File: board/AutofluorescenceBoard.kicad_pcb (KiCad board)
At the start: 2 copper layers, 57.2 x 45.7 mm, 41 parts, among them J1 2002411212, Q1 BSS138, U1 PAM2863ECR, U2 PAM2863ECR, U3 PAM2863ECR

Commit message: Silkscreens :)
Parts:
- added G***: LOGO, LOGO, F.Cu at (146.6, 137.6)
- added G***: LOGO, LOGO, F.Cu at (137.9, 116.7)

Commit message: Layout Changes from CDR
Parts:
- R3: value 0.3 -> 0.15
- R8: value 1K -> 10K
- moved G*** 81.4 mm to (67.5, 118.6)
- moved CR2 63.7 mm to (182.4, 130.1), turned to 90 degrees
- moved D3 61.7 mm to (185.7, 116.0)
- moved D2 56.8 mm to (180.5, 112.0)
- moved Conn1 56.5 mm to (208.7, 105.9)
- moved L2 55.9 mm to (179.8, 120.9)
- moved FanConn1 55.6 mm to (209.8, 121.0)
- moved G*** 55.6 mm to (82.6, 111.3)
- moved D1 54.2 mm to (179.2, 106.2)
- moved D4 54.2 mm to (179.4, 98.6)
- moved R1 54.2 mm to (163.8, 107.0)
- moved R4 54.2 mm to (160.7, 112.8)
- moved C1 54.2 mm to (166.9, 125.5)
- moved C3 54.2 mm to (168.9, 113.4)
- moved CR1 54.2 mm to (158.4, 118.0)
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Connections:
- J1 pad 2: Net-(J1-Pad2) -> unconnected-(J1-Pad2)
- MOSFET1 pad 5: Net-(J1-Pad2) -> GND
- MOSFET1 pad 6: Net-(J1-Pad2) -> GND
- MOSFET1 pad 7: Net-(J1-Pad2) -> GND
- MOSFET1 pad 8: Net-(J1-Pad2) -> GND
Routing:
- net Net-(J1-Pad2): track 28.6 -> 0.00 mm
- net (no net): track 0.00 -> 28.6 mm
- net Net-(D2-Pad2): track 4.06 -> 12.3 mm
- net Net-(D3-Pad2): track 5.74 -> 1.40 mm
- net White LED: track 5.69 -> 9.63 mm
- net ISET 490nm: track 39.5 -> 42.3 mm
- net ISET 405nm: track 59.9 -> 62.6 mm
- net Net-(D2-Pad1): track 7.21 -> 5.32 mm
- net ISET 365nm: track 77.1 -> 78.4 mm
- net +12V: track 179.2 -> 177.9 mm
- net Net-(D3-Pad1): track 6.24 -> 5.22 mm
- net Net-(CR2-Pad2): track 10.6 -> 9.77 mm
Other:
- board size 57.2 x 45.7 mm -> 60.3 x 48.9 mm
- board text removed: "increase width by .01 increase length by .03"

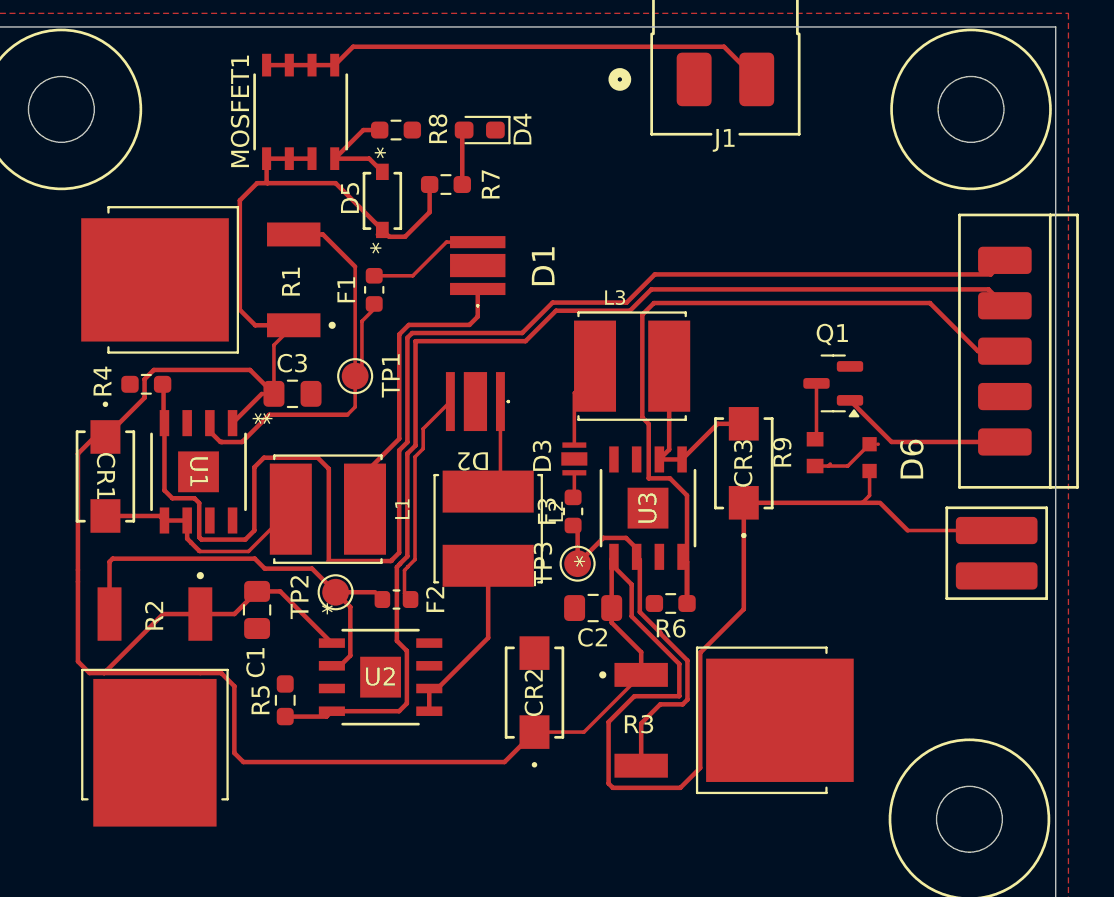
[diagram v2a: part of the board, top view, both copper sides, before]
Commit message: Fixed Connection Issues
MOSFET was messed up, fixed grounding things, and made all traces at least 10 mils.
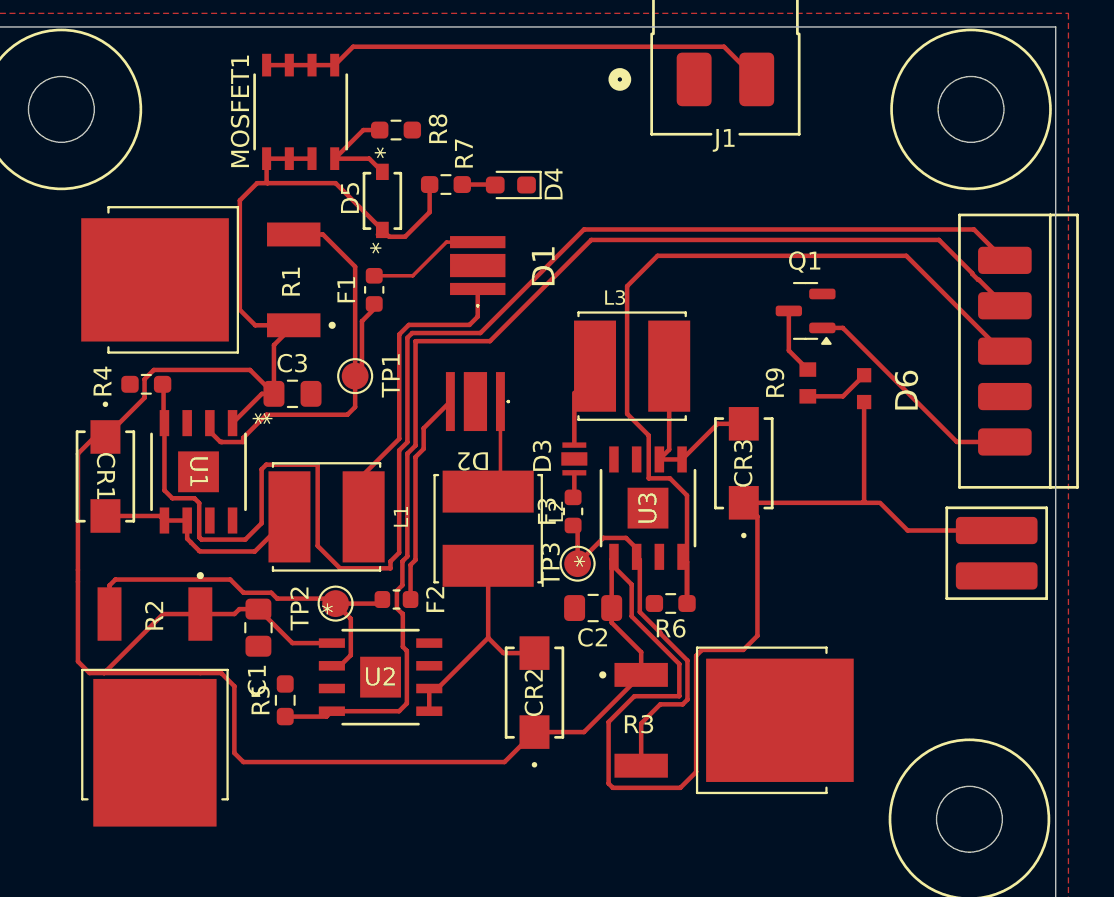
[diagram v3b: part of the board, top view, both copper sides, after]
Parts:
- moved Q1 4.34 mm to (197.6, 108.7)
- moved R9 3.92 mm to (197.7, 112.8)
- moved D6 3.87 mm to (200.9, 113.1)
- moved D4 3.53 mm to (181.1, 101.7)
- moved C1 0.99 mm to (167.0, 126.4)
- moved TP2 0.64 mm to (171.3, 125.1)
- moved L1 0.44 mm to (170.8, 120.2)
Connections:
- J1 pad 2: unconnected-(J1-Pad2) -> Net-(J1-Pad2)
- MOSFET1 pad 5: GND -> Net-(J1-Pad2)
- MOSFET1 pad 6: GND -> Net-(J1-Pad2)
- MOSFET1 pad 7: GND -> Net-(J1-Pad2)
- MOSFET1 pad 8: GND -> Net-(J1-Pad2)
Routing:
- net Net-(J1-Pad2): track 0.00 -> 28.6 mm
- net (no net): track 28.6 -> 0.00 mm
- net +12V: track 177.9 -> 182.8 mm
- net ISET 490nm: track 42.3 -> 46.6 mm
- net White LED: track 9.63 -> 12.9 mm
- net Net-(CR2-Pad2): track 9.77 -> 12.7 mm
- net ISET 405nm: track 62.6 -> 64.9 mm
- net Net-(U2-ISENSE): track 25.5 -> 23.4 mm
- net Net-(D4-A): track 3.09 -> 1.86 mm
- net ISET 365nm: track 78.4 -> 79.4 mm
- net Net-(D1-Pad1): track 18.1 -> 17.4 mm
- net Net-(Q1-D): track 3.16 -> 3.72 mm

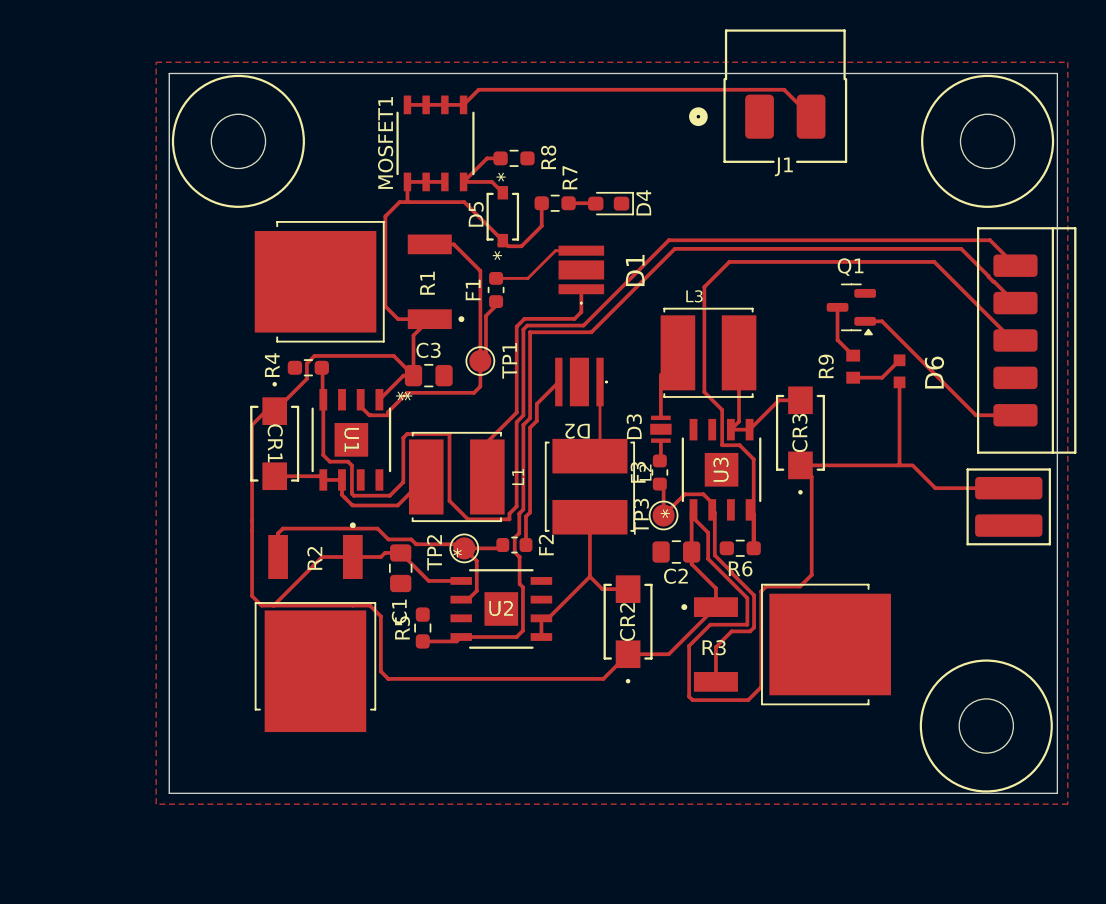
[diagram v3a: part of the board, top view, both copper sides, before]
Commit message: Confined leds white and UV to .25 in radius
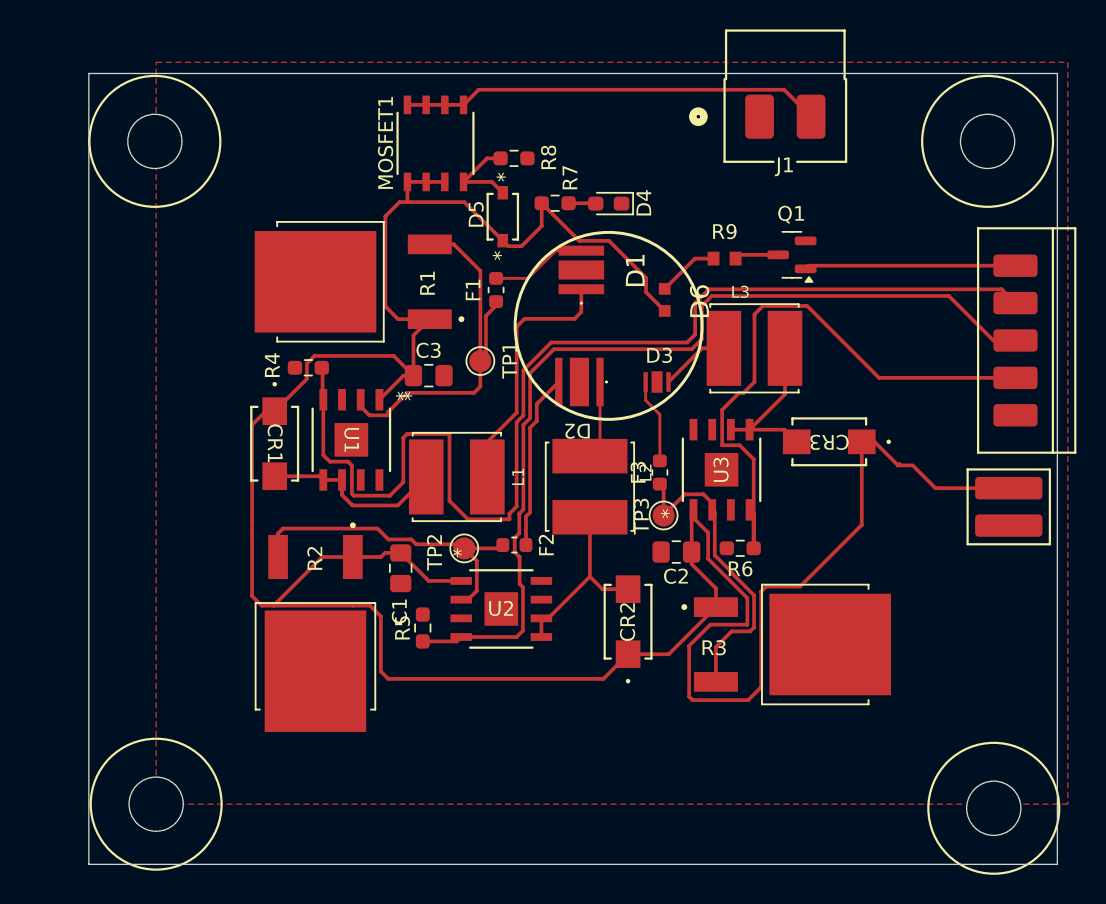
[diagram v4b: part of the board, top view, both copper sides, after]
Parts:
- added H4: MountingHole, MRDT_Drill_Holes:6_32_Hole_Corner, F.Cu at (145.9, 146.9)
- moved D6 16.7 mm to (184.9, 108.2)
- moved R9 11.4 mm to (189.0, 105.4), turned to 0 degrees
- moved H2 5.68 mm to (154.7, 101.9)
- moved H3 5.61 mm to (202.8, 138.3)
- moved Q1 5.39 mm to (193.5, 105.2)
- moved L3 3.14 mm to (191.0, 111.5)
- moved CR3 2.05 mm to (196.1, 117.9), turned to 180 degrees
- moved D3 1.24 mm to (185.4, 114.8), turned to 180 degrees
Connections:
- Conn1 pad 1: ISET 365nm -> White LED
- Conn1 pad 2: ISET 405nm -> ISET 365nm
- Conn1 pad 3: ISET 490nm -> ISET 405nm
- Conn1 pad 4: GND -> ISET 490nm
- Conn1 pad 5: White LED -> GND
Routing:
- net +12V: track 182.8 -> 188.4 mm
- net ISET 490nm: track 46.6 -> 41.3 mm
- net Net-(D3-Pad2): track 1.40 -> 5.86 mm
- net ISET 365nm: track 79.4 -> 77.4 mm
- net ISET 405nm: track 64.9 -> 63.0 mm
- net White LED: track 12.9 -> 14.3 mm
- net Net-(CR3-Pad2): track 11.0 -> 12.0 mm
- net Net-(Q1-D): track 3.72 -> 2.99 mm
- net Net-(D3-Pad1): track 5.22 -> 5.81 mm
- net Net-(D6-K): track 3.64 -> 4.17 mm
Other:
- board size 60.3 x 48.9 mm -> 65.8 x 53.7 mm

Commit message: Add Mitchell's signature
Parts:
- added G***: LOGO, LOGO, F.Cu at (182.4, 139.3)

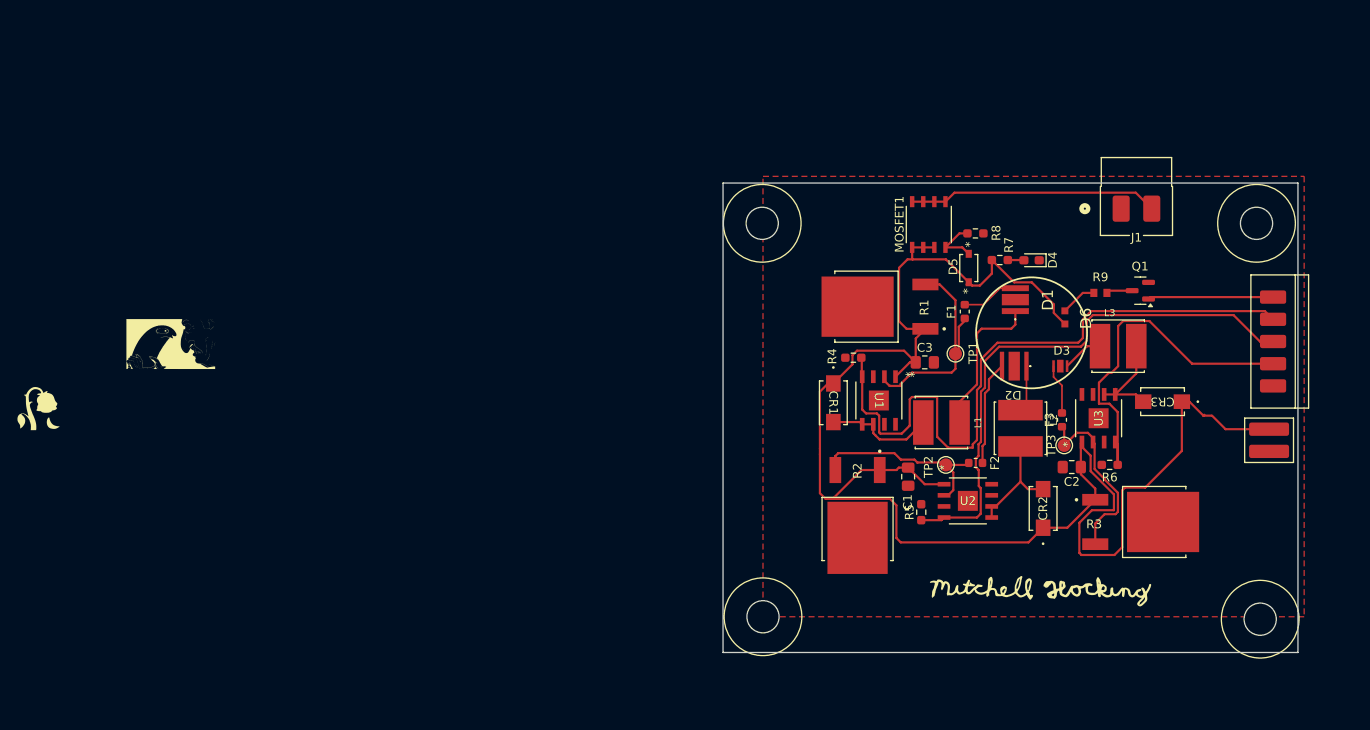
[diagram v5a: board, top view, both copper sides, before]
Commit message: Added Silkscreen drawing
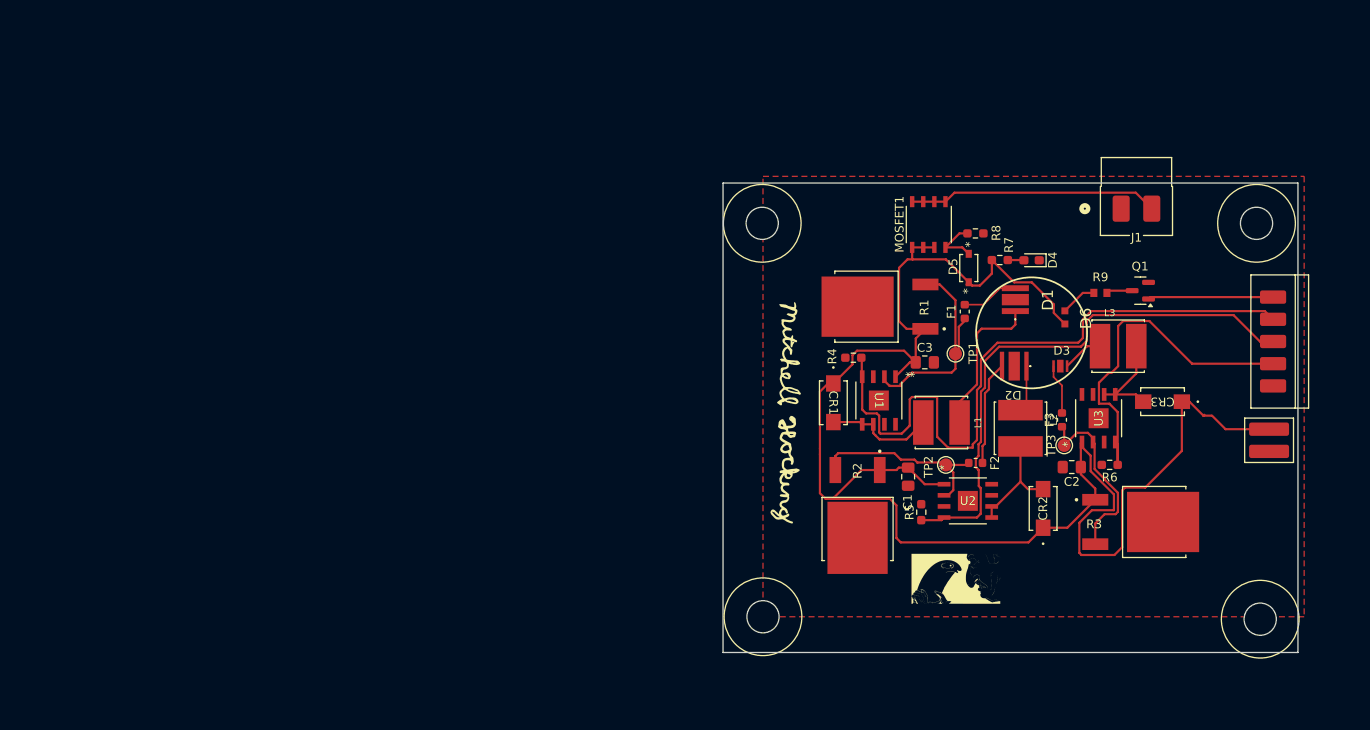
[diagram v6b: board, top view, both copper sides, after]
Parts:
- removed the G*** at (67.5, 118.6)
- moved G*** 93.8 mm to (172.4, 138.1)
- moved G*** 35.3 mm to (153.2, 119.4), turned to -90 degrees

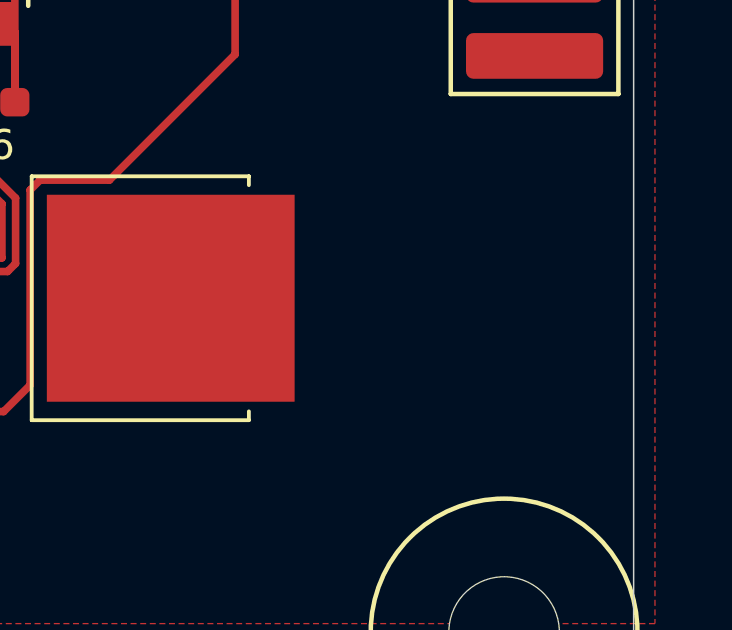
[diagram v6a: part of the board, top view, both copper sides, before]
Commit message: Added back the wilted rose silkscreen
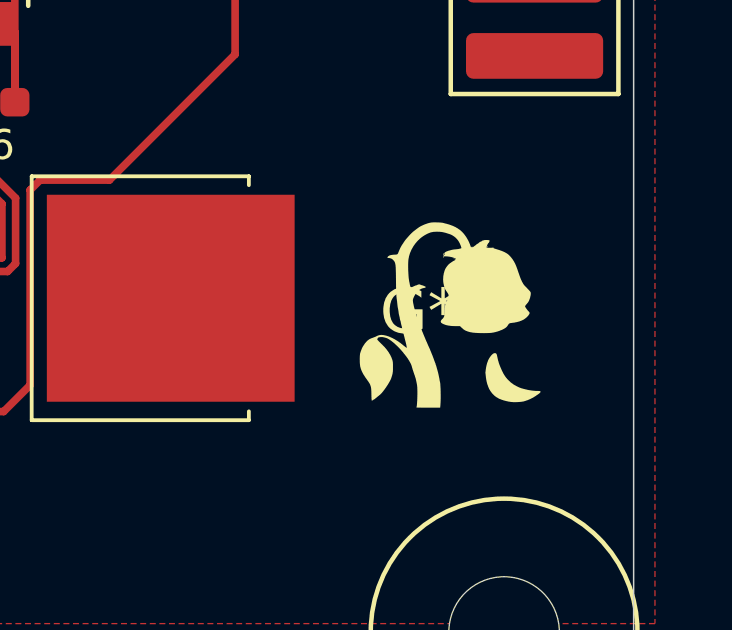
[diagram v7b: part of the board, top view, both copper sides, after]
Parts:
- added G***: LOGO, LOGO, F.Cu at (205.5, 132.1)
